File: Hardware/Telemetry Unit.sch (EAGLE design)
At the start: 53 parts, among them IC1 MEGA128-A, IC2 FT232RL, J2 503182-1852, J3 10118193-0001LF, Q1 10MHz, U1 MPL3115A2, U2 AOZ1280, U3 ICM-20649

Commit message: Update EAGLE and improve silkscreen
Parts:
- FIX, PWR: device led:LEDSML0603 -> led:LEDCHIP-LED0603
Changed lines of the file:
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@@
 <?xml version="1.0" encoding="utf-8"?>
 <!DOCTYPE eagle SYSTEM "eagle.dtd">
-<eagle version="9.4.0">
+<eagle version="9.4.2">
 <drawing>
 <settings>
@@
 <part name="L1" library="TrackerPeripherals" deviceset="L_SMALL" device="L0603" value="1.8n"/>
 <part name="GND1" library="supply1" library_urn="urn:adsk.eagle:library:371" deviceset="GND" device=""/>
-<part name="FIX" library="led" library_urn="urn:adsk.eagle:library:259" deviceset="LED" device="SML0603" package3d_urn="urn:adsk.eagle:package:15832/1"/>
+<part name="FIX" library="led" library_urn="urn:adsk.eagle:library:259" deviceset="LED" device="CHIP-LED0603" package3d_urn="urn:adsk.eagle:package:15819/3"/>
 <part name="R2" library="resistor" library_urn="urn:adsk.eagle:library:348" deviceset="R-US_" device="R0603" package3d_urn="urn:adsk.eagle:package:23555/3" value="1k"/>
 <part name="GND8" library="supply1" library_urn="urn:adsk.eagle:library:371" deviceset="GND" device=""/>
@@
 <part name="C9" library="resistor" library_urn="urn:adsk.eagle:library:348" deviceset="C-US" device="C0805" package3d_urn="urn:adsk.eagle:package:23617/2" value="22u"/>
 <part name="C10" library="resistor" library_urn="urn:adsk.eagle:library:348" deviceset="C-US" device="C0805" package3d_urn="urn:adsk.eagle:package:23617/2" value="22u"/>
-<part name="PWR" library="led" library_urn="urn:adsk.eagle:library:259" deviceset="LED" device="SML0603" package3d_urn="urn:adsk.eagle:package:15832/1"/>
+<part name="PWR" library="led" library_urn="urn:adsk.eagle:library:259" deviceset="LED" device="CHIP-LED0603" package3d_urn="urn:adsk.eagle:package:15819/3"/>
 <part name="R11" library="resistor" library_urn="urn:adsk.eagle:library:348" deviceset="R-US_" device="R0603" package3d_urn="urn:adsk.eagle:package:23555/3" value="1k"/>
 <part name="GND12" library="supply1" library_urn="urn:adsk.eagle:library:371" deviceset="GND" device=""/>

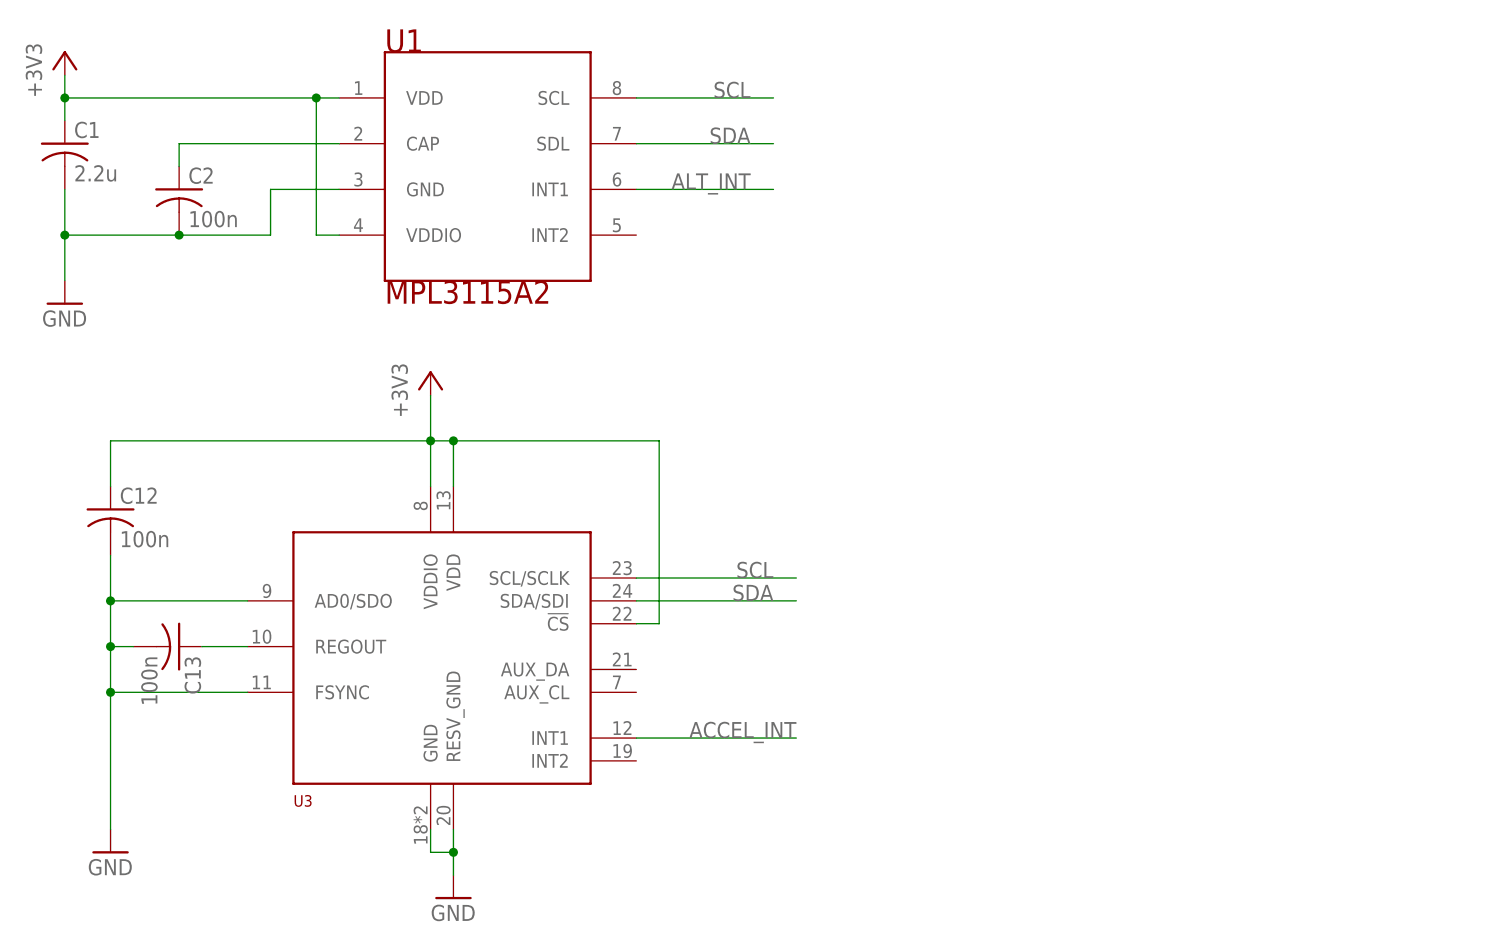
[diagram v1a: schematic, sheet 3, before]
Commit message: Switch Accelerometer
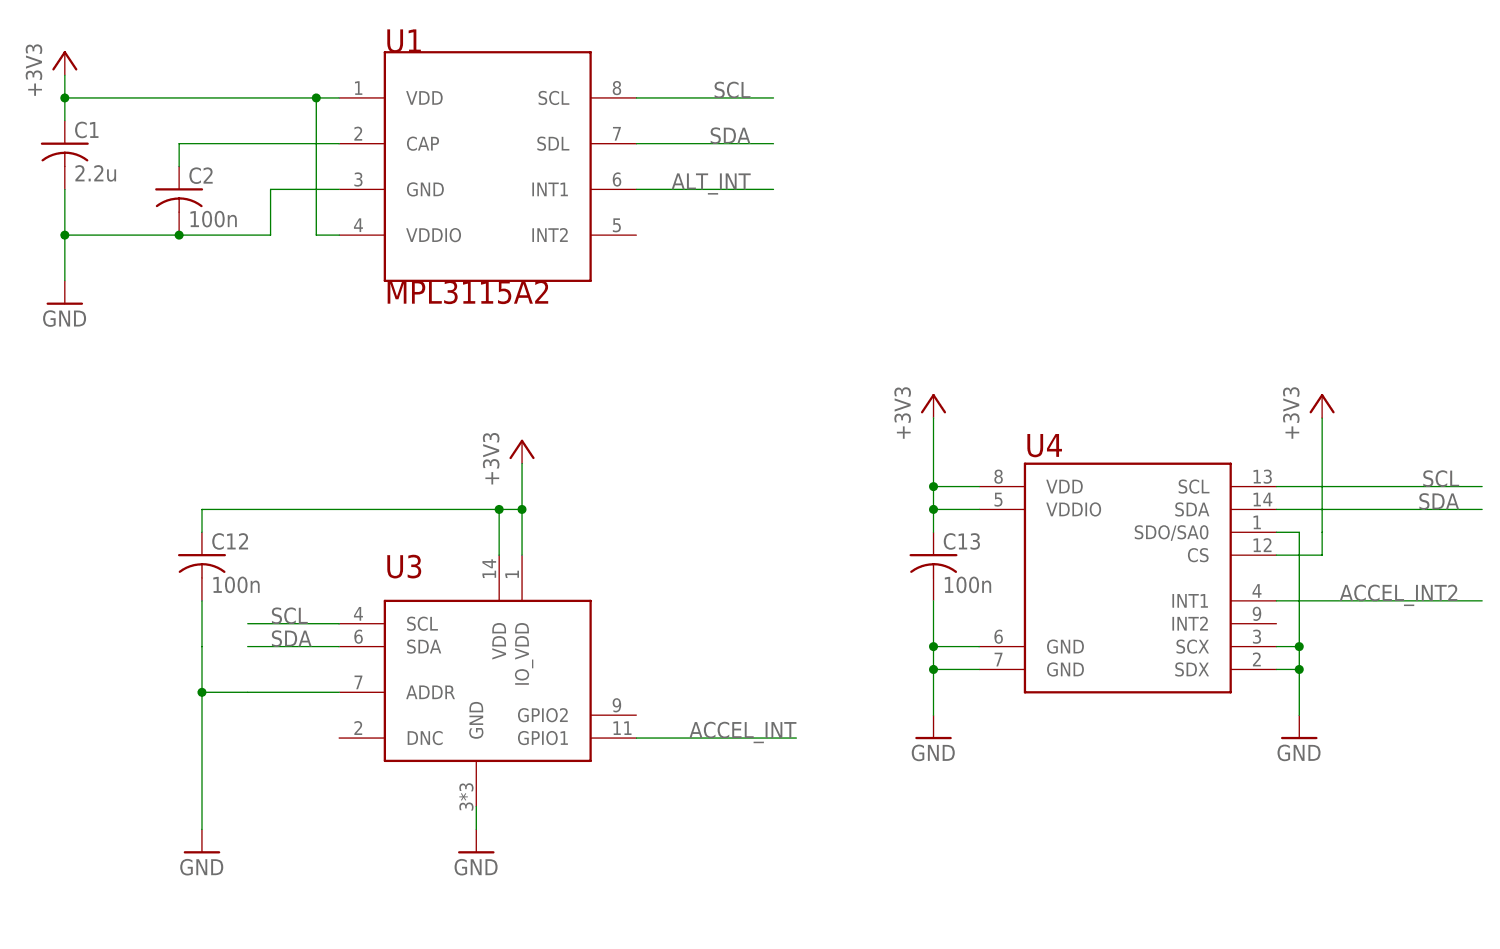
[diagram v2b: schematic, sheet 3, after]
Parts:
- added U4: LSM6DS3, TrackerPeripherals:LSM6DS3
- U3: value ICM-20649 -> KMX63-1055; device TrackerPeripherals:ICM-20649 -> TrackerPeripherals:KMX63-1055
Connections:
- removed net N$8: C13.1, U3.REGOUT
- new net ACCEL_INT2: IC1.(OC3C/INT5)PE5, U4.INT1
- net +3V3: now also C13.1, U3.IO_VDD, U4.CS, U4.VDD, U4.VDDIO; no longer U3.!CS, U3.VDDIO
- net ACCEL_INT: now also U3.GPIO1; no longer U3.INT1
- net GND: now also U3.ADDR, U4.GND@1, U4.GND@2, U4.SCX, U4.SDO/SA0, U4.SDX; no longer U3.AD0/SDO, U3.FSYNC, U3.RESV_GND
- net SCL: now also U3.SCL, U4.SCL; no longer U3.SCL/SCLK
- net SDA: now also U3.SDA, U4.SDA; no longer U3.SDA/SDI
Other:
- moved on the sheet: C12, C13

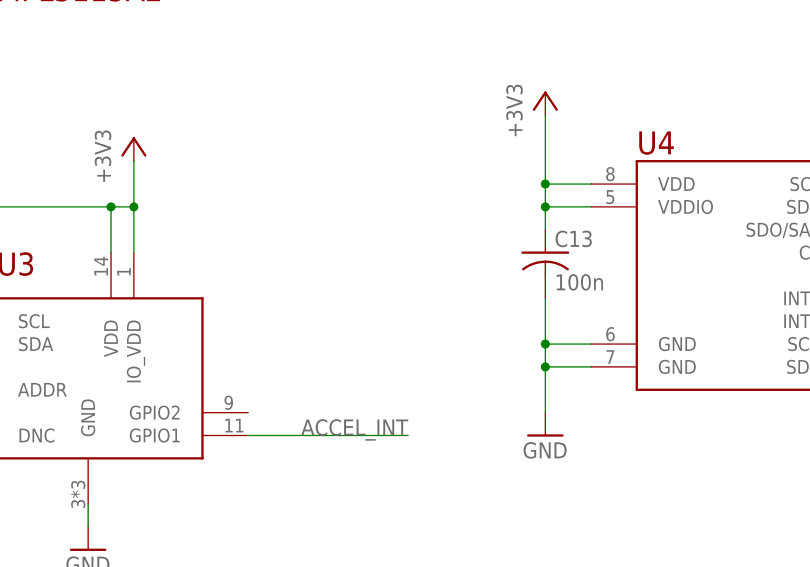
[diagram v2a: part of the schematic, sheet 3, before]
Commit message: Layout accelerometers
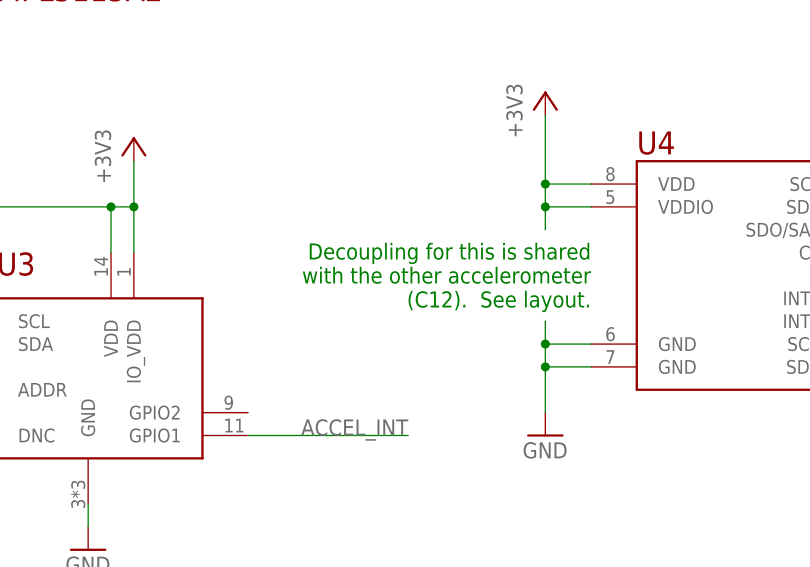
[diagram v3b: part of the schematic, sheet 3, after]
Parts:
- removed C13: 100n, resistor:C-USC0603
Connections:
- net +3V3: no longer C13.1
- net GND: no longer C13.2
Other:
- note added: "Decoupling for this is shared with the other accelerometer (C12). See layout."
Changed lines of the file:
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@@
 <part name="U3" library="TrackerPeripherals" deviceset="KMX63-1055" device=""/>
 <part name="U4" library="TrackerPeripherals" deviceset="LSM6DS3" device=""/>
-<part name="C13" library="resistor" library_urn="urn:adsk.eagle:library:348" deviceset="C-US" device="C0603" package3d_urn="urn:adsk.eagle:package:23616/2" value="100n"/>
 <part name="+3V10" library="supply1" library_urn="urn:adsk.eagle:library:371" deviceset="+3V3" device=""/>
 <part name="GND21" library="supply1" library_urn="urn:adsk.eagle:library:371" deviceset="GND" device=""/>
@@
 <description>Misc Sensing</description>
 <plain>
+<text x="124.46" y="27.94" size="1.778" layer="91" align="center-right">Decoupling for this is shared
+with the other accelerometer
+(C12).  See layout.</text>
 </plain>
 <instances>
@@
 <instance part="U4" gate="G$1" x="139.7" y="27.94" smashed="yes">
 <attribute name="NAME" x="129.54" y="41.402" size="2.54" layer="94"/>
-</instance>
-<instance part="C13" gate="G$1" x="119.38" y="30.48" smashed="yes">
-<attribute name="NAME" x="120.396" y="31.115" size="1.778" layer="95"/>
-<attribute name="VALUE" x="120.396" y="26.289" size="1.778" layer="96"/>
 </instance>
 <instance part="+3V10" gate="G$1" x="119.38" y="48.26" smashed="yes">
@@
 <segment>
 <pinref part="+3V10" gate="G$1" pin="+3V3"/>
-<pinref part="C13" gate="G$1" pin="1"/>
 <wire x1="119.38" y1="45.72" x2="119.38" y2="38.1" width="0.1524" layer="91"/>
 <pinref part="U4" gate="G$1" pin="VDDIO"/>
@@
 <segment>
 <pinref part="GND21" gate="1" pin="GND"/>
-<pinref part="C13" gate="G$1" pin="2"/>
 <wire x1="119.38" y1="12.7" x2="119.38" y2="17.78" width="0.1524" layer="91"/>
 <pinref part="U4" gate="G$1" pin="GND@1"/>
 <wire x1="119.38" y1="17.78" x2="119.38" y2="20.32" width="0.1524" layer="91"/>
-<wire x1="119.38" y1="20.32" x2="119.38" y2="25.4" width="0.1524" layer="91"/>
+<wire x1="119.38" y1="20.32" x2="119.38" y2="22.86" width="0.1524" layer="91"/>
 <wire x1="124.46" y1="20.32" x2="119.38" y2="20.32" width="0.1524" layer="91"/>
 <junction x="119.38" y="20.32"/>

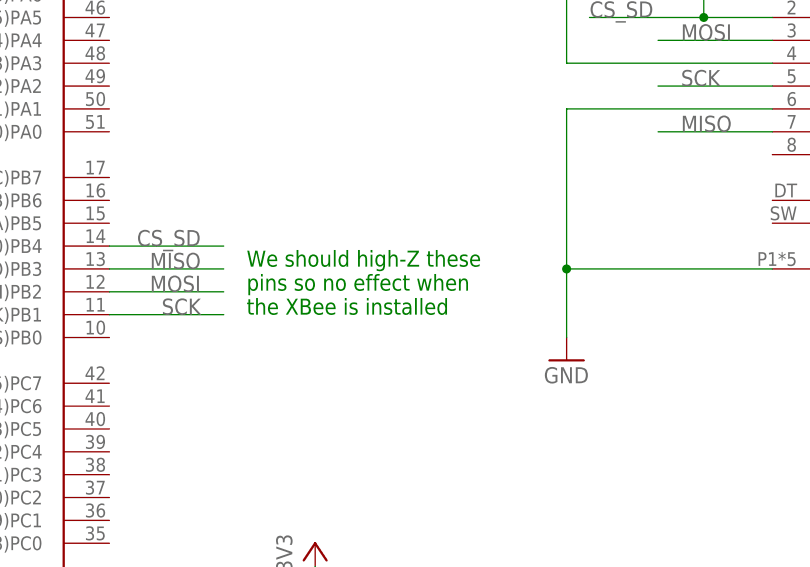
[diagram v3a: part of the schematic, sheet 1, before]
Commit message: Removed old comment which was no longer relevant
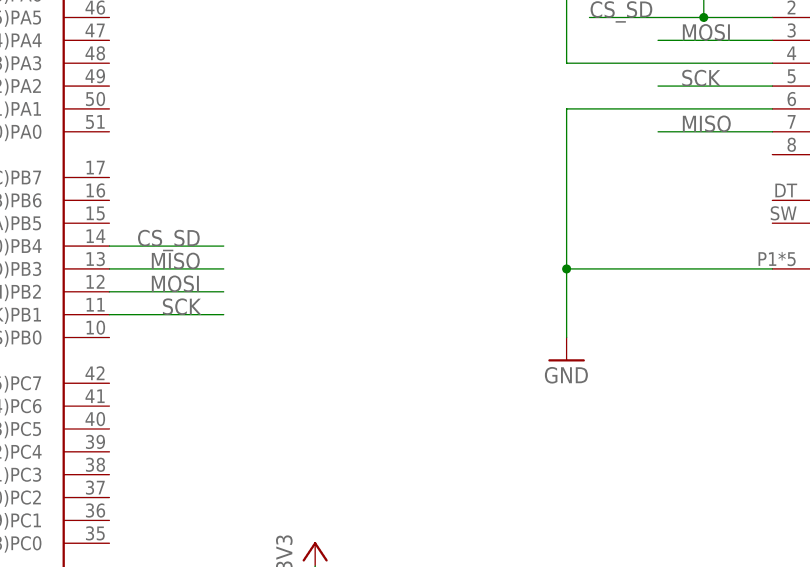
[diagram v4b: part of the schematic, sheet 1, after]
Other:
- note removed: "We should high-Z these pins so no effect when the XBee is installed"
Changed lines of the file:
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@@
 <description>ATMega128 Microcontroller</description>
 <plain>
-<text x="93.98" y="76.2" size="1.778" layer="91">We should high-Z these
-pins so no effect when
-the XBee is installed</text>
 <text x="-22.86" y="10.16" size="1.778" layer="91" align="center-left">0.25 attenuation with 2.56V
 ADC reference = 1mV per bit

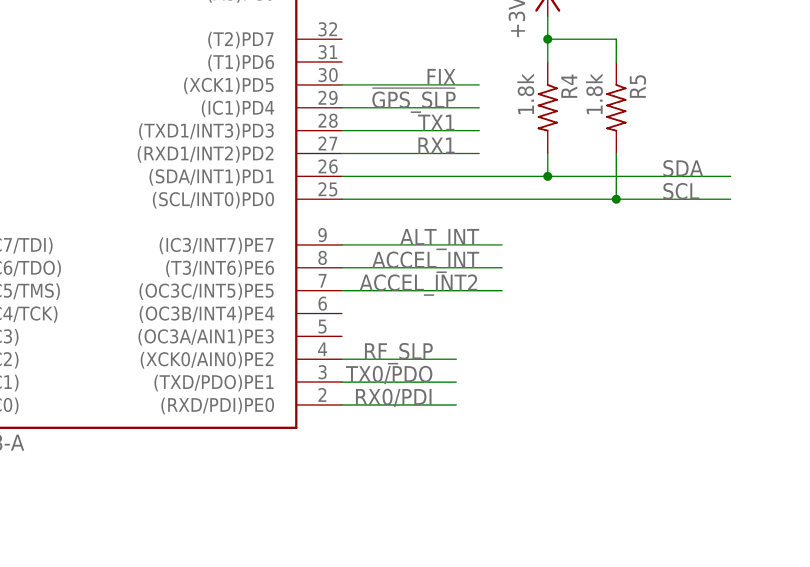
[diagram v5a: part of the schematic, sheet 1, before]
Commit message: Create updated pin mapping header
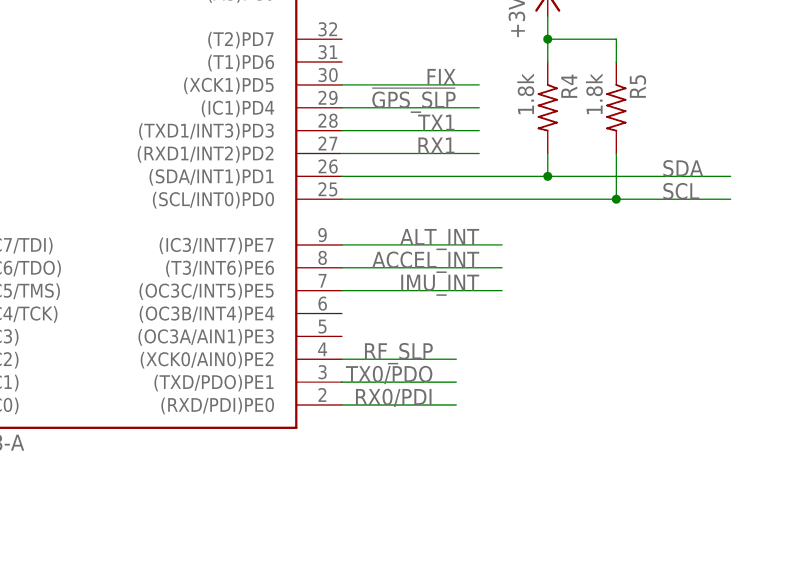
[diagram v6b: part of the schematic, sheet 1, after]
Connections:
- net ACCEL_INT2 renamed IMU_INT
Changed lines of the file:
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@@
 </segment>
 </net>
-<net name="ACCEL_INT2" class="0">
+<net name="IMU_INT" class="0">
 <segment>
 <label x="93.98" y="17.78" size="1.778" layer="95" align="bottom-right"/>
@@
 </segment>
 </net>
-<net name="ACCEL_INT2" class="0">
+<net name="IMU_INT" class="0">
 <segment>
 <pinref part="U4" gate="G$1" pin="INT1"/>
